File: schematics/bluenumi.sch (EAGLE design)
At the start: 48 parts, among them IC1 MEGA8-P, J1 POWER_JACKPTH, Q1 16Mhz, Q3 BC337

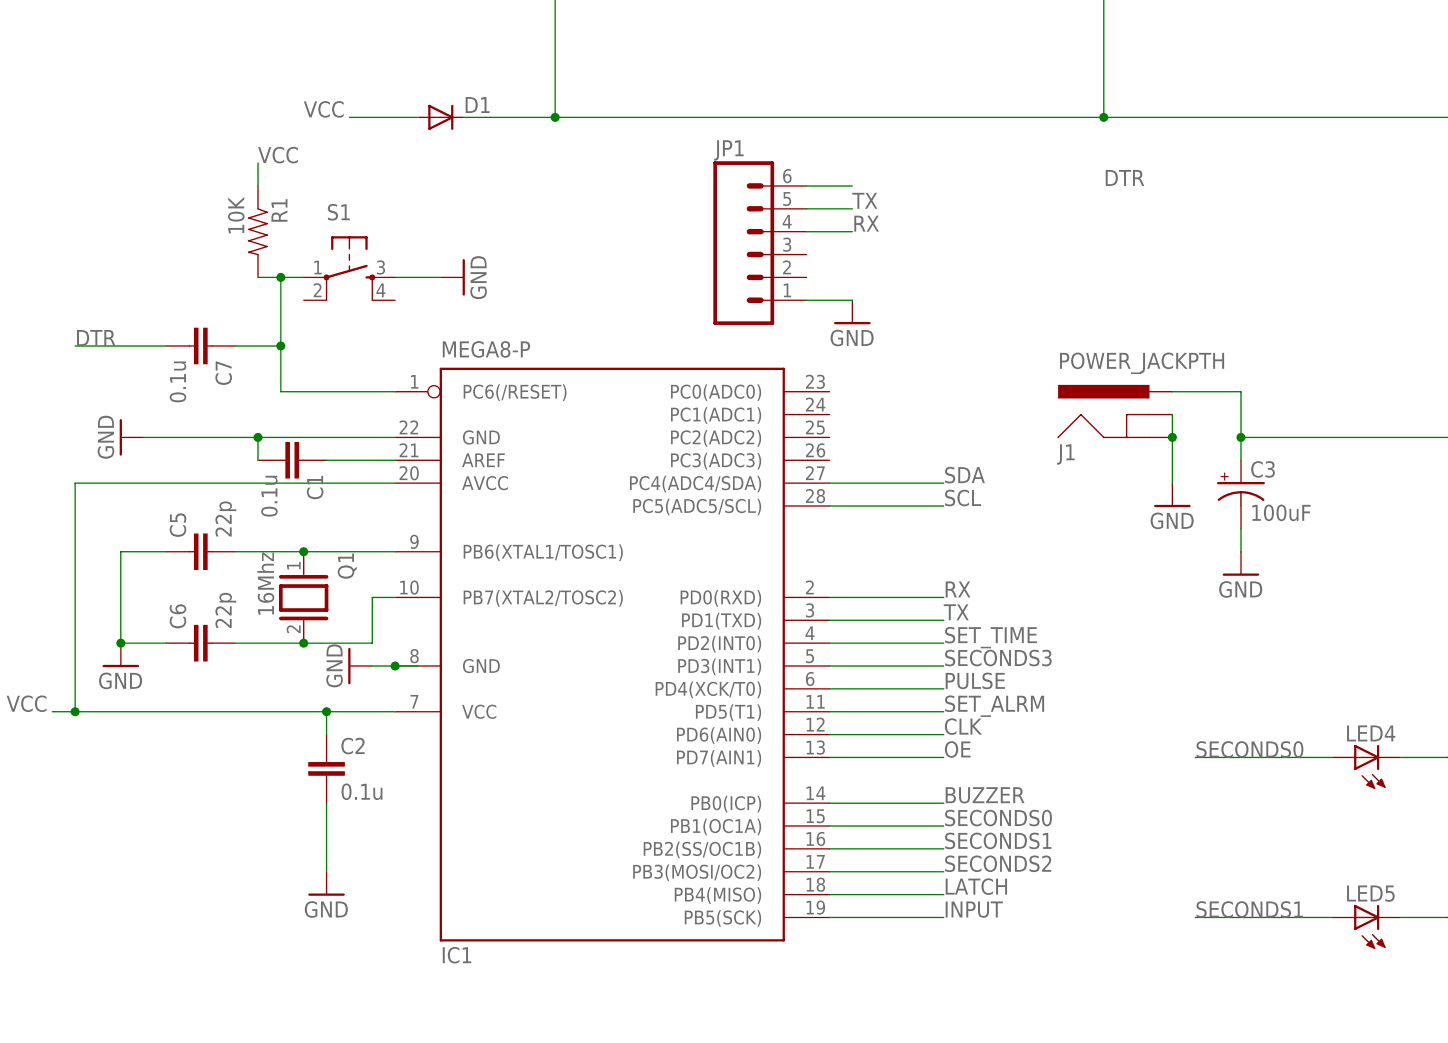
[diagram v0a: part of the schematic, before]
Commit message: Create gerber files Update board and schematic so that LED PWM is not on Arduino pins 3 or 11
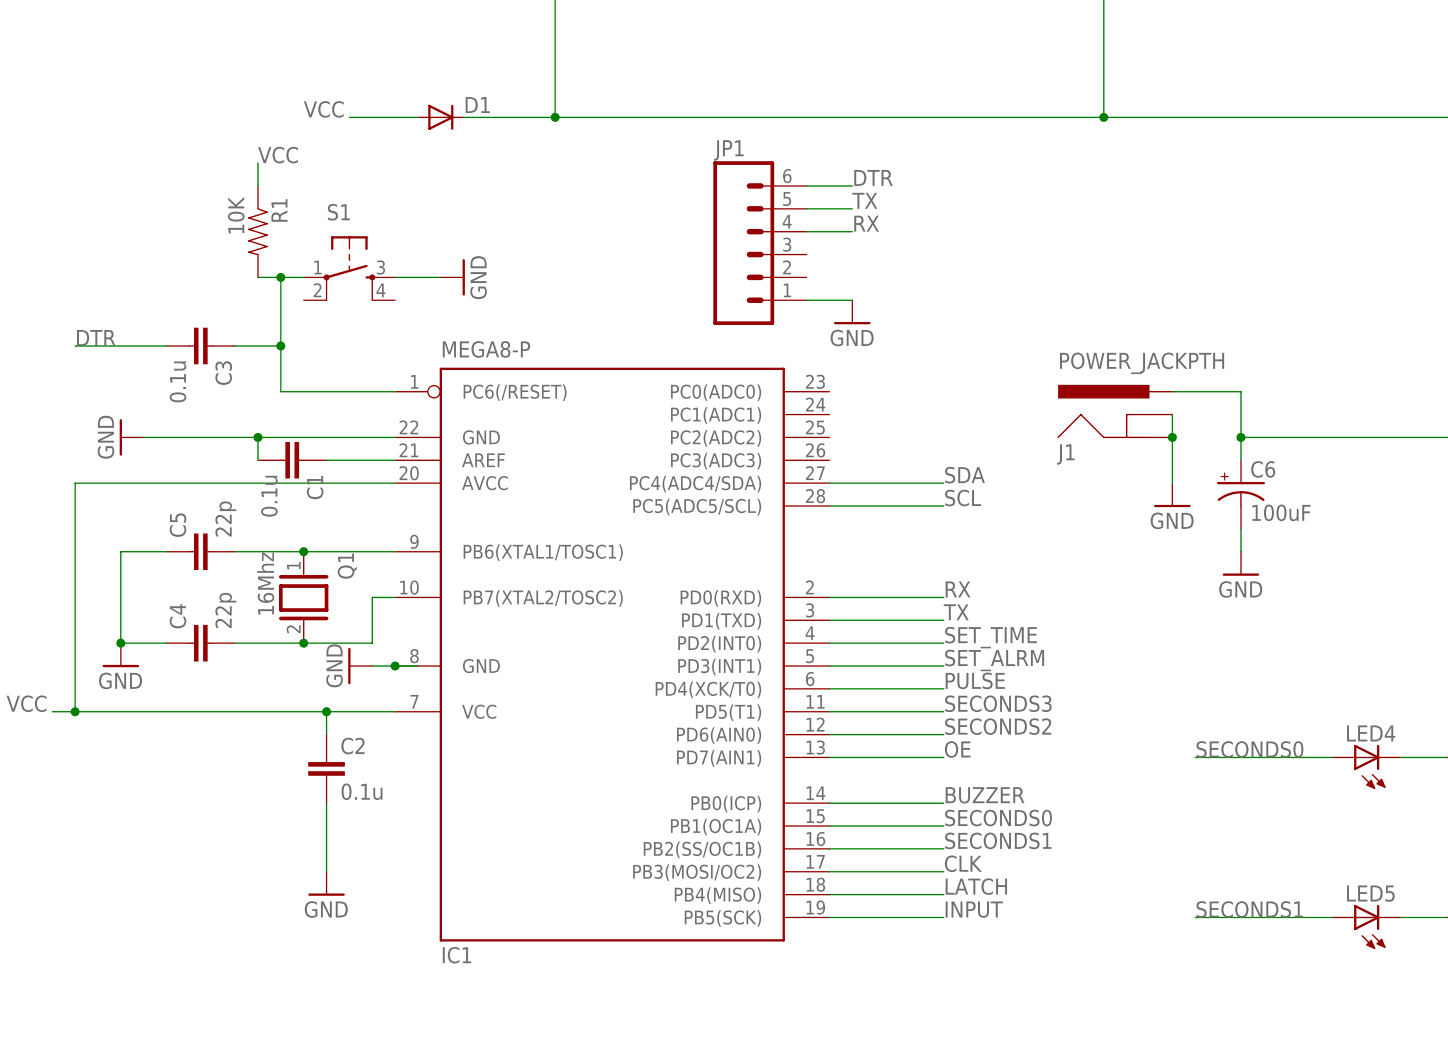
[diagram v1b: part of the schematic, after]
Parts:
- removed C7: 0.1u, SparkFun:CAPPTH
- added C4: 22p, SparkFun:CAPPTH
- C3: value 100uF -> 0.1u; device SparkFun:CAP_POLPTH2 -> SparkFun:CAPPTH
- C6: value 22p -> 100uF; device SparkFun:CAPPTH -> SparkFun:CAP_POLPTH2
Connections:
- net CLK: now also IC1.PB3(MOSI/OC2); no longer IC1.PD6(AIN0)
- net DTR: now also C3.2; no longer C7.2
- net GND: now also C4.1, C6.-; no longer C3.-, C6.1
- net N$22: now also C4.2; no longer C6.2
- net N$23: now also C3.1; no longer C7.1
- net SECONDS2: now also IC1.PD6(AIN0); no longer IC1.PB3(MOSI/OC2)
- net SECONDS3: now also IC1.PD5(T1); no longer IC1.PD3(INT1)
- net SET_ALRM: now also IC1.PD3(INT1); no longer IC1.PD5(T1)
- net VCC: now also C6.+; no longer C3.+
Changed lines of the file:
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@@
 <?xml version="1.0" encoding="utf-8"?>
 <!DOCTYPE eagle SYSTEM "eagle.dtd">
-<eagle version="6.0">
+<eagle version="6.1">
 <drawing>
 <settings>
@@
 <part name="J1" library="SparkFun" deviceset="POWER_JACK" device="PTH"/>
 <part name="C5" library="SparkFun" deviceset="CAP" device="PTH" value="22p"/>
-<part name="C6" library="SparkFun" deviceset="CAP" device="PTH" value="22p"/>
+<part name="C4" library="SparkFun" deviceset="CAP" device="PTH" value="22p"/>
 <part name="GND8" library="SparkFun" deviceset="GND" device=""/>
 <part name="GND9" library="SparkFun" deviceset="GND" device=""/>
@@
 <part name="GND14" library="SparkFun" deviceset="GND" device=""/>
 <part name="FRAME2" library="frames" deviceset="FRAME_B_L" device=""/>
-<part name="C7" library="SparkFun" deviceset="CAP" device="PTH" value="0.1u"/>
+<part name="C3" library="SparkFun" deviceset="CAP" device="PTH" value="0.1u"/>
 <part name="R6" library="SparkFun" deviceset="RESISTOR" device="PTH1" value="820"/>
 <part name="R7" library="SparkFun" deviceset="RESISTOR" device="PTH1" value="820"/>
@@
 <part name="GND24" library="SparkFun" deviceset="GND" device=""/>
 <part name="R10" library="SparkFun" deviceset="RESISTOR" device="PTH1" value="200"/>
-<part name="C3" library="SparkFun" deviceset="CAP_POL" device="PTH2" value="100uF"/>
+<part name="C6" library="SparkFun" deviceset="CAP_POL" device="PTH2" value="100uF"/>
 <part name="GND5" library="SparkFun" deviceset="GND" device=""/>
 <part name="GND20" library="SparkFun" deviceset="GND" device=""/>
@@
 <instance part="J1" gate="G$1" x="160.02" y="124.46"/>
 <instance part="C5" gate="G$1" x="55.88" y="114.3" rot="R90"/>
-<instance part="C6" gate="G$1" x="55.88" y="104.14" rot="R90"/>
+<instance part="C4" gate="G$1" x="55.88" y="104.14" rot="R90"/>
 <instance part="GND8" gate="1" x="45.72" y="101.6"/>
 <instance part="GND9" gate="1" x="83.82" y="144.78" rot="R90"/>
@@
 <instance part="GND14" gate="1" x="127" y="139.7"/>
 <instance part="FRAME2" gate="G$1" x="0" y="0"/>
-<instance part="FRAME2" gate="G$2" x="317.5" y="0"/>
-<instance part="C7" gate="G$1" x="53.34" y="137.16" rot="R270"/>
+<instance part="FRAME2" gate="G$2" x="326.39" y="0.254"/>
+<instance part="C3" gate="G$1" x="53.34" y="137.16" rot="R270"/>
 <instance part="R6" gate="G$1" x="43.18" y="203.2" rot="R90"/>
 <instance part="R7" gate="G$1" x="104.14" y="203.2" rot="R90"/>
@@
 <instance part="GND24" gate="1" x="177.8" y="50.8" rot="R90"/>
 <instance part="R10" gate="G$1" x="165.1" y="50.8" rot="R180"/>
-<instance part="C3" gate="G$1" x="170.18" y="121.92"/>
+<instance part="C6" gate="G$1" x="170.18" y="121.92"/>
 <instance part="GND5" gate="1" x="170.18" y="111.76"/>
 <instance part="GND20" gate="1" x="177.8" y="27.94" rot="R90"/>
@@
 <pinref part="C5" gate="G$1" pin="1"/>
 <pinref part="GND8" gate="1" pin="GND"/>
-<pinref part="C6" gate="G$1" pin="1"/>
+<pinref part="C4" gate="G$1" pin="1"/>
 </segment>
 <segment>
@@
 <segment>
 <wire x1="170.18" y1="116.84" x2="170.18" y2="114.3" width="0.1524" layer="91"/>
-<pinref part="C3" gate="G$1" pin="-"/>
+<pinref part="C6" gate="G$1" pin="-"/>
 <pinref part="GND5" gate="1" pin="GND"/>
 </segment>
@@
 <pinref part="IC1" gate="G$1" pin="PB7(XTAL2/TOSC2)"/>
 <pinref part="Q1" gate="G$1" pin="2"/>
-<pinref part="C6" gate="G$1" pin="2"/>
+<pinref part="C4" gate="G$1" pin="2"/>
 </segment>
 </net>
@@
 <pinref part="S1" gate="S" pin="1"/>
 <pinref part="IC1" gate="G$1" pin="PC6(/RESET)"/>
-<pinref part="C7" gate="G$1" pin="1"/>
+<pinref part="C3" gate="G$1" pin="1"/>
 </segment>
 </net>
@@
 <wire x1="50.8" y1="137.16" x2="40.64" y2="137.16" width="0.1524" layer="91"/>
 <label x="40.64" y="137.16" size="1.778" layer="95"/>
-<pinref part="C7" gate="G$1" pin="2"/>
+<pinref part="C3" gate="G$1" pin="2"/>
 </segment>
 <segment>
 <wire x1="121.92" y1="154.94" x2="127" y2="154.94" width="0.1524" layer="91"/>
-<label x="154.94" y="154.94" size="1.778" layer="95"/>
+<label x="127" y="154.94" size="1.778" layer="95"/>
 <pinref part="JP1" gate="G$1" pin="6"/>
 </segment>
@@
 <junction x="170.18" y="127"/>
 <label x="198.12" y="127" size="1.778" layer="95"/>
-<pinref part="C3" gate="G$1" pin="+"/>
+<pinref part="C6" gate="G$1" pin="+"/>
 <pinref part="J1" gate="G$1" pin="PWR"/>
 </segment>
@@
 </segment>
 <segment>
+<wire x1="124.46" y1="93.98" x2="137.16" y2="93.98" width="0.1524" layer="91"/>
+<label x="137.16" y="93.98" size="1.778" layer="95"/>
+<pinref part="IC1" gate="G$1" pin="PD6(AIN0)"/>
+</segment>
+</net>
+<net name="SECONDS3" class="0">
+<segment>
+<wire x1="246.38" y1="73.66" x2="231.14" y2="73.66" width="0.1524" layer="91"/>
+<label x="231.14" y="73.66" size="1.778" layer="95"/>
+<pinref part="LED7" gate="G$1" pin="A"/>
+</segment>
+<segment>
+<wire x1="124.46" y1="96.52" x2="137.16" y2="96.52" width="0.1524" layer="91"/>
+<label x="137.16" y="96.52" size="1.778" layer="95"/>
+<pinref part="IC1" gate="G$1" pin="PD5(T1)"/>
+</segment>
+</net>
+<net name="CLK" class="0">
+<segment>
+<wire x1="45.72" y1="231.14" x2="38.1" y2="231.14" width="0.1524" layer="91"/>
+<label x="38.1" y="231.14" size="1.778" layer="95"/>
+<pinref part="U$1" gate="G$1" pin="CLK"/>
+</segment>
+<segment>
+<wire x1="106.68" y1="231.14" x2="99.06" y2="231.14" width="0.1524" layer="91"/>
+<label x="99.06" y="231.14" size="1.778" layer="95"/>
+<pinref part="U$2" gate="G$1" pin="CLK"/>
+</segment>
+<segment>
+<wire x1="167.64" y1="231.14" x2="160.02" y2="231.14" width="0.1524" layer="91"/>
+<label x="160.02" y="231.14" size="1.778" layer="95"/>
+<pinref part="U$3" gate="G$1" pin="CLK"/>
+</segment>
+<segment>
+<wire x1="231.14" y1="231.14" x2="223.52" y2="231.14" width="0.1524" layer="91"/>
+<label x="223.52" y="231.14" size="1.778" layer="95"/>
+<pinref part="U$4" gate="G$1" pin="CLK"/>
+</segment>
+<segment>
 <wire x1="124.46" y1="78.74" x2="137.16" y2="78.74" width="0.1524" layer="91"/>
 <label x="137.16" y="78.74" size="1.778" layer="95"/>
 <pinref part="IC1" gate="G$1" pin="PB3(MOSI/OC2)"/>
-</segment>
-</net>
-<net name="SECONDS3" class="0">
-<segment>
-<wire x1="246.38" y1="73.66" x2="231.14" y2="73.66" width="0.1524" layer="91"/>
-<label x="231.14" y="73.66" size="1.778" layer="95"/>
-<pinref part="LED7" gate="G$1" pin="A"/>
-</segment>
-<segment>
-<wire x1="124.46" y1="101.6" x2="137.16" y2="101.6" width="0.1524" layer="91"/>
-<label x="137.16" y="101.6" size="1.778" layer="95"/>
-<pinref part="IC1" gate="G$1" pin="PD3(INT1)"/>
-</segment>
-</net>
-<net name="CLK" class="0">
-<segment>
-<wire x1="45.72" y1="231.14" x2="38.1" y2="231.14" width="0.1524" layer="91"/>
-<label x="38.1" y="231.14" size="1.778" layer="95"/>
-<pinref part="U$1" gate="G$1" pin="CLK"/>
-</segment>
-<segment>
-<wire x1="106.68" y1="231.14" x2="99.06" y2="231.14" width="0.1524" layer="91"/>
-<label x="99.06" y="231.14" size="1.778" layer="95"/>
-<pinref part="U$2" gate="G$1" pin="CLK"/>
-</segment>
-<segment>
-<wire x1="167.64" y1="231.14" x2="160.02" y2="231.14" width="0.1524" layer="91"/>
-<label x="160.02" y="231.14" size="1.778" layer="95"/>
-<pinref part="U$3" gate="G$1" pin="CLK"/>
-</segment>
-<segment>
-<wire x1="231.14" y1="231.14" x2="223.52" y2="231.14" width="0.1524" layer="91"/>
-<label x="223.52" y="231.14" size="1.778" layer="95"/>
-<pinref part="U$4" gate="G$1" pin="CLK"/>
-</segment>
-<segment>
-<wire x1="124.46" y1="93.98" x2="137.16" y2="93.98" width="0.1524" layer="91"/>
-<label x="137.16" y="93.98" size="1.778" layer="95"/>
-<pinref part="IC1" gate="G$1" pin="PD6(AIN0)"/>
 </segment>
 </net>
@@
 <net name="SET_ALRM" class="0">
 <segment>
-<wire x1="124.46" y1="96.52" x2="137.16" y2="96.52" width="0.1524" layer="91"/>
-<label x="137.16" y="96.52" size="1.778" layer="95"/>
-<pinref part="IC1" gate="G$1" pin="PD5(T1)"/>
-</segment>
-<segment>
 <wire x1="144.78" y1="20.32" x2="116.84" y2="20.32" width="0.1524" layer="91"/>
 <label x="116.84" y="20.32" size="1.778" layer="95"/>
 <pinref part="U$7" gate="G$1" pin="S1"/>
 </segment>
-</net>
+<segment>
+<wire x1="124.46" y1="101.6" x2="137.16" y2="101.6" width="0.1524" layer="91"/>
+<label x="137.16" y="101.6" size="1.778" layer="95"/>
+<pinref part="IC1" gate="G$1" pin="PD3(INT1)"/>
+</segment>
+</net>
